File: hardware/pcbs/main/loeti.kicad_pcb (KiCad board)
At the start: 4 copper layers, 80 x 50.5 mm, 99 parts, among them J1 REDFIT_SWD_6, J2 DATA, J3 POWER, J4 Conn_01x04_Pin, Q1 Si4162DY, Q2 BC817, Q4 BC817, Q5 BC807, Q6 Si4425FDY, SW1 BOOT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

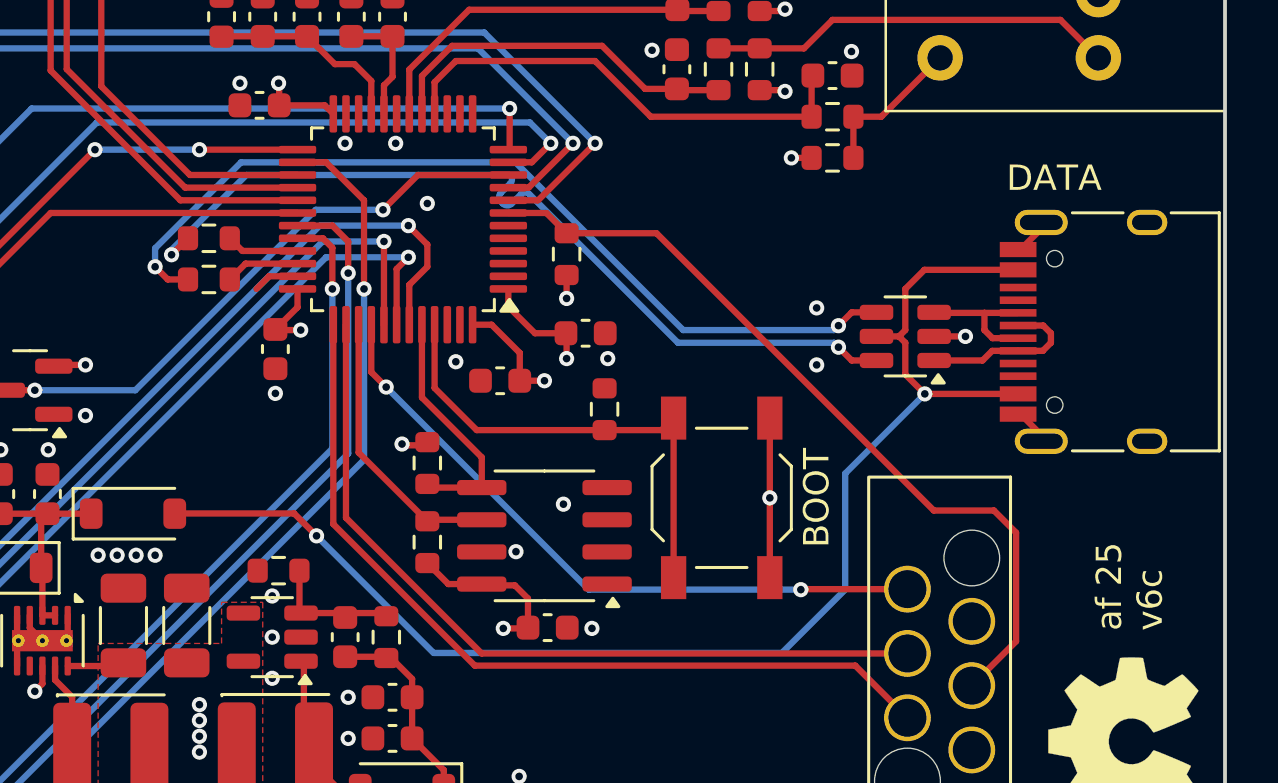
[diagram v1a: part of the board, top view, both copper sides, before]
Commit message: fix: v6d hardware, CC resistors on data port
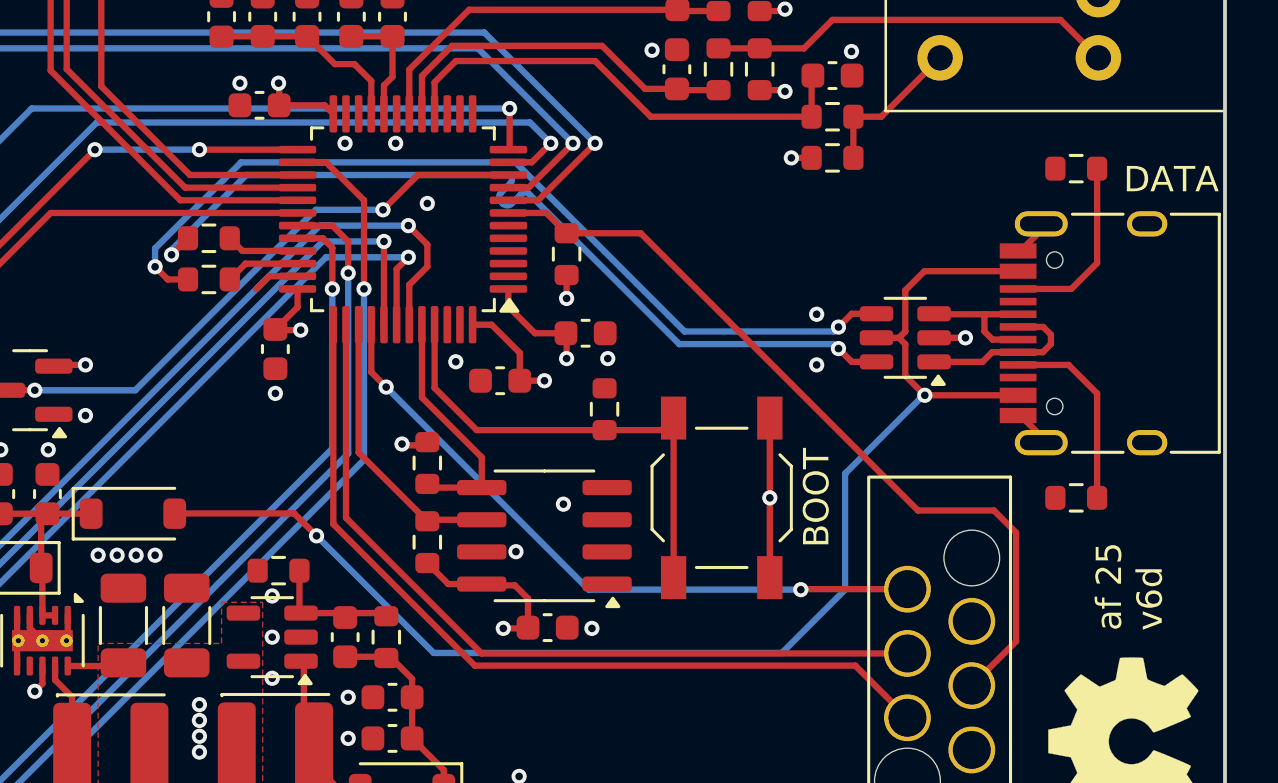
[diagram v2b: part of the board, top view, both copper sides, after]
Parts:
- added R33: 5.1k, Resistor_SMD:R_0603_1608Metric, F.Cu at (181.0, 102.2)
- added R34: 5.1k, Resistor_SMD:R_0603_1608Metric, F.Cu at (181.0, 89.2)
- moved J2 0.06 mm to (182.8, 95.8)
- moved U1 0.06 mm to (174.2, 95.9)
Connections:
- J2 pad A5: unconnected-(J2-CC1-PadA5) -> Net-(J2-CC1)
- J2 pad B5: unconnected-(J2-CC2-PadB5) -> Net-(J2-CC2)
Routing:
- net Net-(J2-CC1): track 0.00 -> 7.71 mm
- net Net-(J2-CC2): track 0.00 -> 7.27 mm
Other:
- board text added: "af 25 v6d"
- board text removed: "af 25 v6c"

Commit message: feat: sleep support on PCB
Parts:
- added D9: BAT54S, Package_TO_SOT_SMD:SOT-23, F.Cu at (167.0, 89.5)
- added R35: 10k, Resistor_SMD:R_0603_1608Metric, F.Cu at (164.2, 89.0)
- added R36: 10k, Resistor_SMD:R_0603_1608Metric, F.Cu at (167.0, 92.5)
- added TP1: SLP, TestPoint:TestPoint_Plated_Hole_D2.0mm, F.Cu at (175.2, 89.8)
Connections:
- net /ADC2_IN1 renamed /ADC1_IN1
- net /ADC2_IN2 renamed /ADC1_IN2
- R34 pad 1: GND -> Net-(J2-CC2)
- R34 pad 2: Net-(J2-CC2) -> GND
- U4 pad 13: unconnected-(U4-PA5-Pad13) -> /SLP
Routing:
- net Net-(R35-Pad1): track 0.00 -> 14.7 mm
- net /SLP: track 0.00 -> 12.3 mm
- net +3V3: track 58.0 -> 61.2 mm, vias 25 -> 26
- net GND: vias 54 -> 55

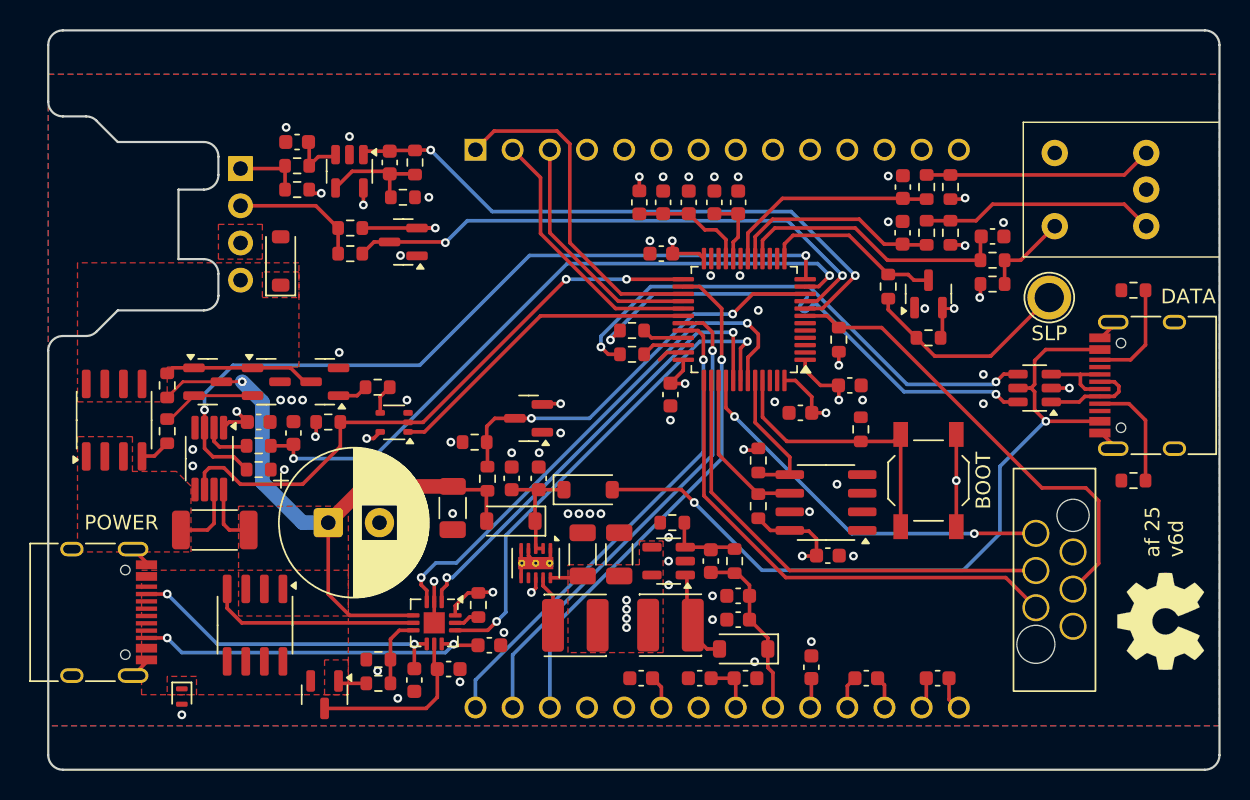
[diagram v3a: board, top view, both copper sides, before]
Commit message: feat: update to 5-pin XLR for sleep
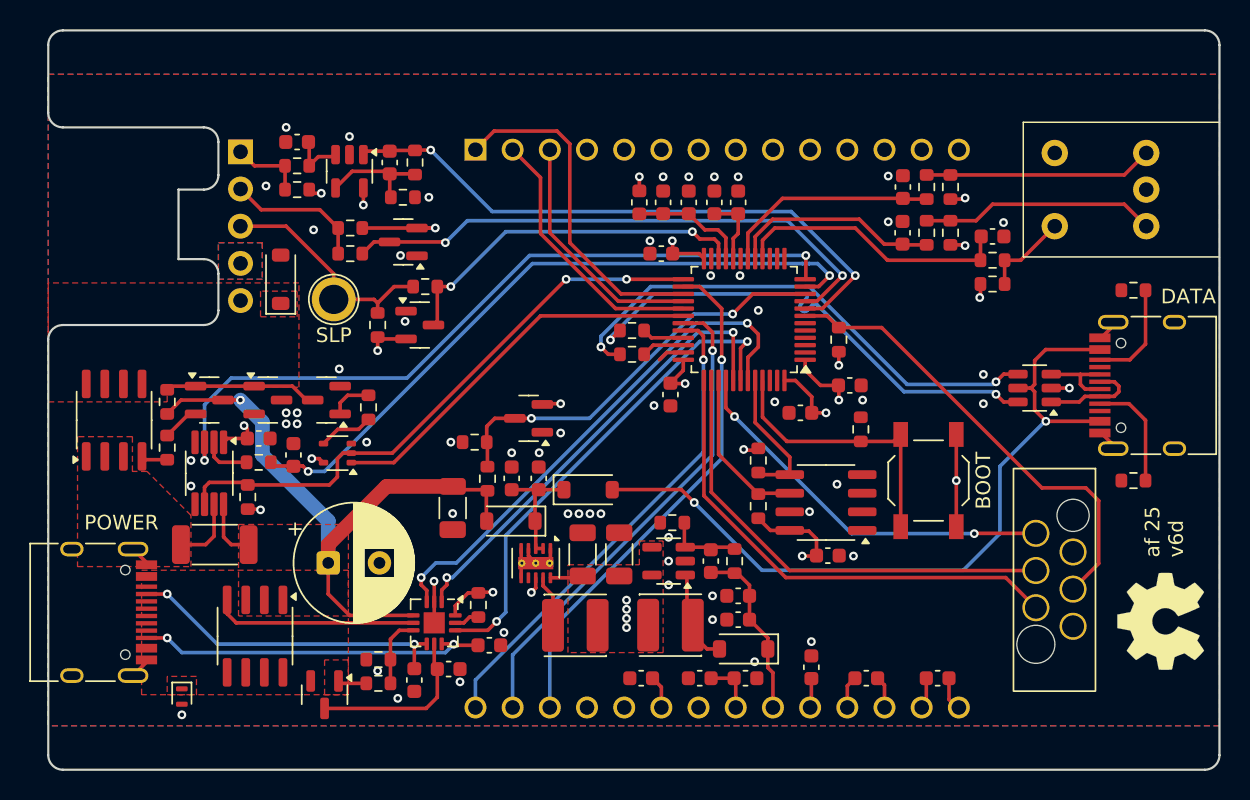
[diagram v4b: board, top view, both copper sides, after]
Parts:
- removed J4: Conn_01x04_Pin, Connector_PinHeader_2.54mm:PinHeader_1x04_P2.54mm_Horizontal
- removed R29: 25k, Resistor_SMD:R_0603_1608Metric
- added J5: Conn_01x05_Pin, Connector_PinHeader_2.54mm:PinHeader_1x05_P2.54mm_Horizontal, B.Cu at (120.0, 79.8)
- C26: footprint Capacitor_THT:CP_Radial_D10.0mm_P3.50mm -> Capacitor_THT:CP_Radial_D8.0mm_P3.50mm
- moved TP1 48.9 mm to (126.4, 89.9)
- moved R36 37.6 mm to (129.4, 91.6), turned to 90 degrees
- moved D9 34.8 mm to (132.2, 91.6), turned to 0 degrees
- moved R35 31.6 mm to (132.6, 89.0), turned to 0 degrees
- moved R30 7.52 mm to (120.5, 103.4), turned to -90 degrees
- moved U6 4.41 mm to (126.6, 100.4)
- moved C26 2.75 mm to (126.0, 107.9)
- moved R22 1.51 mm to (128.8, 97.2), turned to 90 degrees
- moved C33 1.50 mm to (123.6, 100.5)
- moved Q2 1.25 mm to (117.9, 96.8)
- moved Q4 1.25 mm to (125.9, 96.8)
- moved Q5 1.25 mm to (121.9, 96.8)
- moved D5 1.25 mm to (122.8, 88.5)
- moved C34 1.12 mm to (121.2, 99.4)
- moved R18 1.12 mm to (115.0, 96.9)
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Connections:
- net Net-(R35-Pad1) renamed /SLP_EXT
- U4 pad 13: /SLP -> unconnected-(U4-PA5-Pad13)
- U4 pad 22: unconnected-(U4-PB10-Pad22) -> /SLP
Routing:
- net /SLP: track 12.3 -> 24.9 mm, vias 0 -> 2
- net /TIM1_CH1: track 22.1 -> 26.8 mm
- net Net-(Q2-E): track 6.26 -> 2.09 mm
- net Net-(R22-Pad1): track 2.02 -> 3.76 mm
- net /DAC1_OUT1: track 53.7 -> 52.0 mm
- net /SLP_EXT: track 14.7 -> 16.1 mm
- net /CURR_ALERT: track 41.2 -> 40.4 mm
- net +3V3: track 61.2 -> 60.5 mm
- net VDC: track 47.8 -> 47.0 mm
- net /TC+: track 4.35 -> 5.06 mm
- net Net-(Q4-B): track 2.08 -> 2.66 mm
- net Net-(Q1-G): track 14.4 -> 13.9 mm
- net GND: vias 55 -> 57
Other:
- outline, holes or cut-outs redrawn
- board text added: "+14,500 mm from center"
- board text added: "-1,000 mm from center"
- board text added: "-11,875 mm from center"
- board text added: "-14,375 mm from center"

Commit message: feat: v7a initial hardware design
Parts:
- removed C30: ~, Capacitor_SMD:C_0603_1608Metric
- removed U11: TLV333DBV, Package_TO_SOT_SMD:SOT-23-5
- added C2: 100n, Capacitor_SMD:C_0603_1608Metric, F.Cu at (133.4, 85.2)
- added D10: BAT54S, Package_TO_SOT_SMD:SOT-23, F.Cu at (138.1, 85.3)
- added R29: 220k, Resistor_SMD:R_0603_1608Metric, F.Cu at (126.0, 91.1)
- added R37: 220k, Resistor_SMD:R_0603_1608Metric, F.Cu at (126.9, 85.2)
- added R38: 1k, Resistor_SMD:R_0603_1608Metric, F.Cu at (130.1, 85.2)
- added U7: TLV2333, Package_SO:SOIC-8_3.9x4.9mm_P1.27mm, F.Cu at (131.8, 88.9)
- C29: value 330p -> 22p
- Q6: value Si4425FDY -> Si4825
- R23: value 1M -> 22k
- R24: value 10k -> 22k
- R26: value 1k -> 10k
- moved D9 13.4 mm to (130.2, 78.4)
- moved R35 13.4 mm to (130.6, 75.8)
- moved R36 13.4 mm to (127.4, 78.4)
- moved C29 11.5 mm to (138.1, 88.9)
- moved TP1 11.4 mm to (124.0, 78.8), turned to 180 degrees
- moved R26 10.5 mm to (139.8, 88.9), turned to 90 degrees
- moved R25 9.52 mm to (136.5, 88.9), turned to 90 degrees
- moved R23 7.32 mm to (126.0, 89.4)
- moved D2 5.06 mm to (127.2, 82.7)
- moved R10 5.06 mm to (123.6, 83.5)
- moved R9 5.06 mm to (123.6, 81.8)
- moved R24 4.51 mm to (123.6, 85.2)
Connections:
- C29 pad 1: /ADC1_IN1 -> /ADC1_IN2
- C29 pad 2: Net-(U11--) -> Net-(U7B--)
- D2 pad 3: /ADC1_IN2 -> /ADC1_IN1
- D5 pad 1: /HEATER -> /RED
- J5 pad 1: /TC+ -> /SLP_EXT
- J5 pad 3: /SLP_EXT -> /GREEN
- J5 pad 5: /HEATER -> /RED
- Q6 pad 5: /HEATER -> /RED
- Q6 pad 6: /HEATER -> /RED
- Q6 pad 7: /HEATER -> /RED
- Q6 pad 8: /HEATER -> /RED
- R10 pad 2: /ADC1_IN2 -> /ADC1_IN1
- R23 pad 1: +3V3 -> Net-(U7A-+)
- R23 pad 2: /TC+ -> /RED
- R24 pad 1: /TC+ -> /GREEN
- R25 pad 1: /ADC1_IN1 -> Net-(U7B--)
- R25 pad 2: Net-(U11--) -> /ADC1_IN2
- R26 pad 1: Net-(U11--) -> Net-(U7B--)
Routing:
- net Net-(U7B-+): track 0.00 -> 9.20 mm
- net Net-(U11--): track 7.42 -> 0.00 mm
- net Net-(U7B--): track 0.00 -> 5.71 mm
- net /TC+: track 5.06 -> 0.00 mm
- net /DET: track 9.32 -> 4.58 mm
- net /SLP: track 24.9 -> 29.6 mm
- net Net-(U7A-+): track 0.00 -> 4.26 mm
- net /SLP_EXT: track 16.1 -> 11.9 mm
- net Net-(R37-Pad2): track 0.00 -> 3.33 mm
- net Net-(U7A--): track 3.52 -> 6.83 mm
- net /ADC1_IN2: track 38.6 -> 35.4 mm
- net /ADC1_IN1: track 41.5 -> 44.5 mm
- net /GREEN: track 0.00 -> 2.96 mm
- net /RED: track 0.00 -> 2.75 mm
- net +3V3: track 60.5 -> 61.6 mm
- added copper zone on F.Cu, net /RED
- removed copper zone on F.Cu, net /HEATER
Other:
- board text added: "af 25 v7a"
- board text removed: "af 25 v6d"

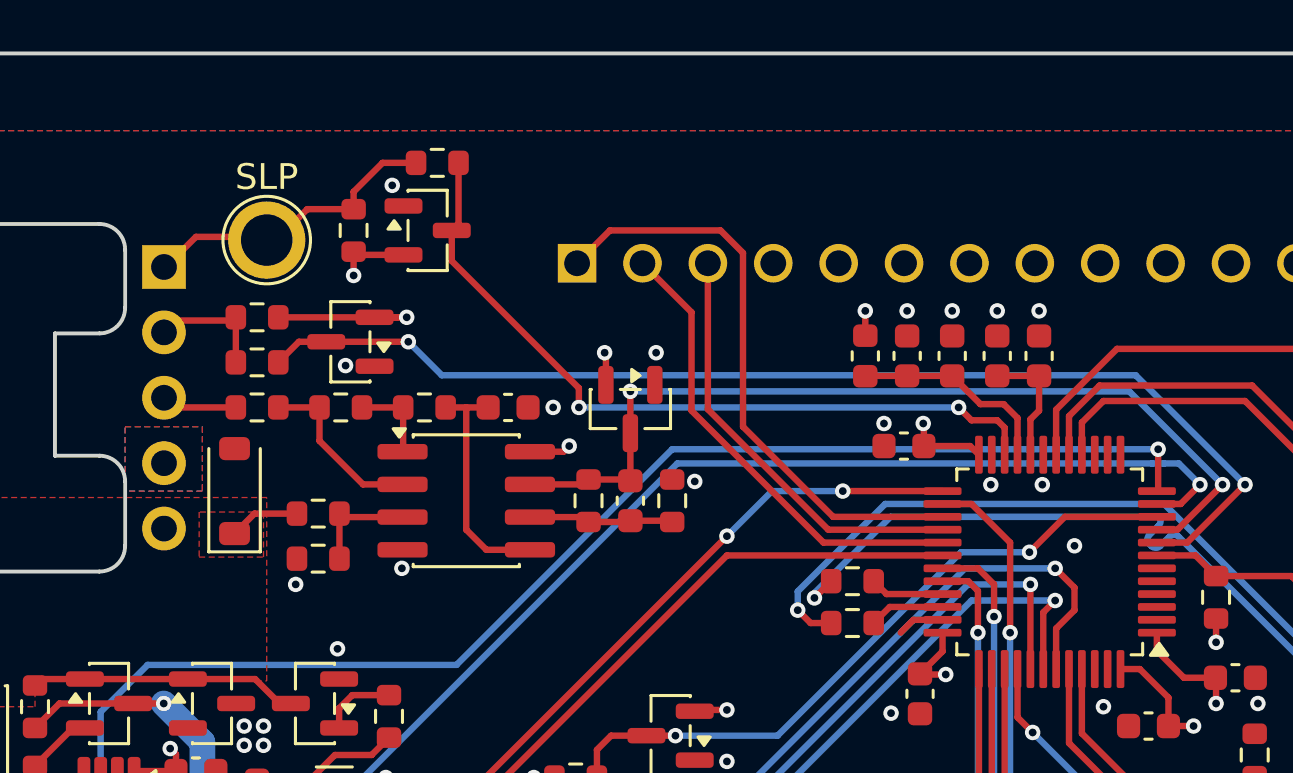
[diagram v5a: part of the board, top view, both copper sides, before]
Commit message: feat: support multiple board variants
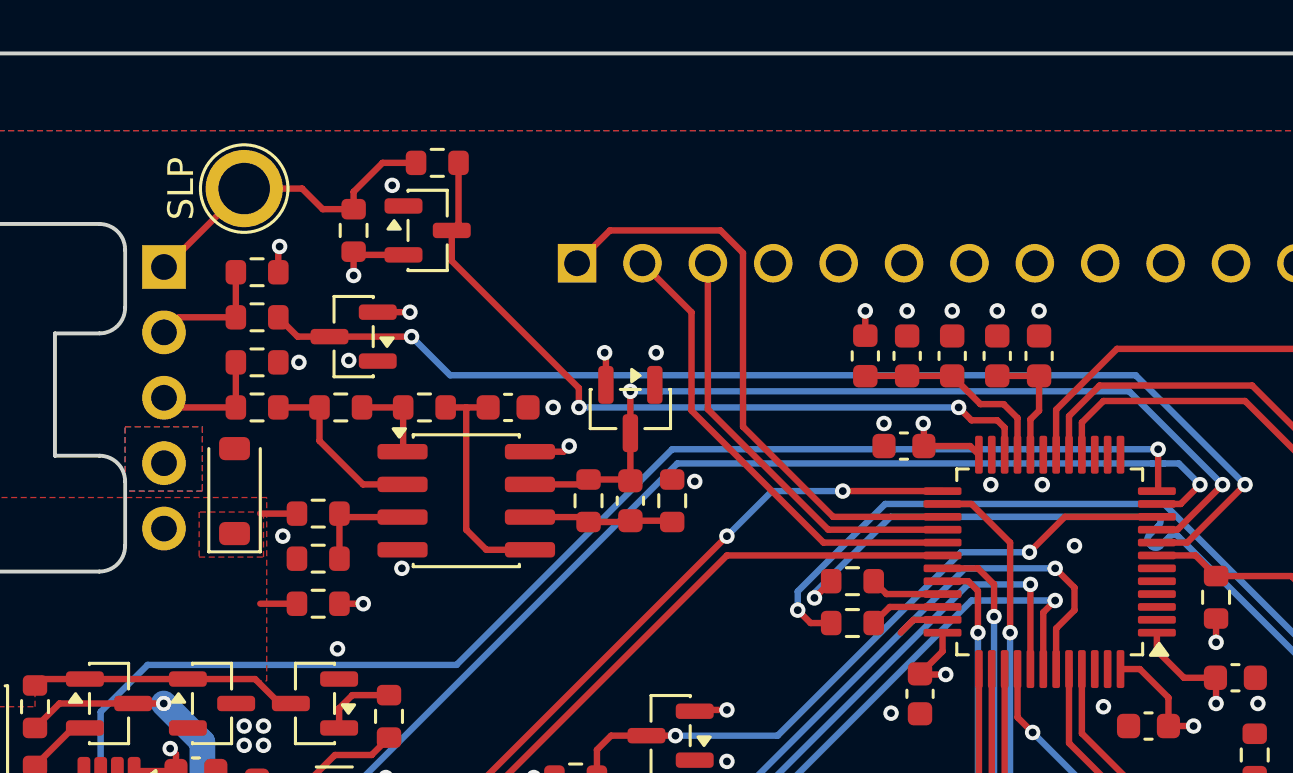
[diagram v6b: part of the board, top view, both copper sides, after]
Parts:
- added R39: 2M, Resistor_SMD:R_0603_1608Metric, F.Cu at (123.6, 83.5)
- added R40: 2M, Resistor_SMD:R_0603_1608Metric, F.Cu at (126.0, 92.9)
- moved TP1 2.18 mm to (123.1, 76.8), turned to -90 degrees
- moved R10 1.75 mm to (123.6, 81.8)
- moved R9 1.75 mm to (123.6, 80.0)
- moved D2 0.24 mm to (127.4, 82.5)
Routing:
- net +3V3: track 61.6 -> 58.8 mm, vias 26 -> 28
- net /GREEN: track 2.96 -> 4.71 mm
- net /SLP_EXT: track 11.9 -> 12.5 mm
- net GND: track 14.6 -> 14.5 mm, vias 57 -> 58

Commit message: feat: hw v7a
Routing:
- net Net-(Q2-E): track 2.09 -> 6.09 mm
- net Net-(U7B--): track 5.71 -> 5.13 mm
- net /GREEN: track 4.71 -> 4.17 mm
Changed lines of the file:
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@@
 			)
 		)
-		(property "Datasheet" "https://www.st.com/resource/en/datasheet/stm32g431cb.pdf"
+		(property "Datasheet" "https://www.st.com/resource/en/datasheet/stm32g491cc.pdf"
 			(at 0 0 0)
 			(layer "F.Fab")
@@
 			)
 		)
-		(property "Description" "STMicroelectronics Arm Cortex-M4 MCU, 128KB flash, 32KB RAM, 170 MHz, 1.71-3.6V, 38 GPIO, LQFP48"
+		(property "Description" "STMicroelectronics Arm Cortex-M4 MCU, 256KB flash, 112KB RAM, 170 MHz, 1.71-3.6V, 38 GPIO, LQFP48"
 			(at 0 0 0)
 			(layer "F.Fab")
@@
 	)
 	(segment
-		(start 129.25 90.805)
-		(end 129.275 90.78)
-		(width 0.25)
-		(layer "F.Cu")
-		(net 2)
-	)
-	(segment
 		(start 175.3875 95.93)
 		(end 176.625 95.93)
@@
 	)
 	(segment
-		(start 136.425 89.625)
-		(end 136.5 89.7)
-		(width 0.25)
-		(layer "F.Cu")
-		(net 7)
-	)
-	(segment
-		(start 139.75 89.625)
-		(end 139.75 89.7)
-		(width 0.25)
-		(layer "F.Cu")
-		(net 7)
-	)
-	(segment
-		(start 139.725 89.65)
-		(end 139.75 89.625)
-		(width 0.25)
-		(layer "F.Cu")
-		(net 7)
-	)
-	(segment
-		(start 136.185 89.51)
-		(end 136.3 89.625)
-		(width 0.25)
-		(layer "F.Cu")
-		(net 7)
-	)
-	(segment
 		(start 134.225 89.51)
 		(end 136.185 89.51)
@@
 	)
 	(segment
-		(start 138.075 89.7)
-		(end 138.125 89.65)
-		(width 0.25)
-		(layer "F.Cu")
-		(net 7)
-	)
-	(segment
 		(start 136.5 89.7)
 		(end 138.075 89.7)
@@
 	)
 	(segment
-		(start 136.3 89.625)
-		(end 136.425 89.625)
-		(width 0.25)
-		(layer "F.Cu")
-		(net 7)
-	)
-	(segment
 		(start 140.175 106.890661)
 		(end 140.675 106.890661)
@@
 	)
 	(segment
+		(start 120.9375 97.7)
+		(end 116.9375 97.7)
+		(width 0.25)
+		(layer "F.Cu")
+		(net 21)
+	)
+	(segment
 		(start 116.475 97.7)
 		(end 115 99.175)
@@
 	)
 	(segment
-		(start 138.125 88.025)
-		(end 138.125 88.1)
-		(width 0.25)
-		(layer "F.Cu")
-		(net 72)
-	)
-	(segment
-		(start 136.5 88.175)
-		(end 136.5 88.05)
-		(width 0.25)
-		(layer "F.Cu")
-		(net 72)
-	)
-	(segment
 		(start 138.125 84.625)
 		(end 138.125 88.1)
@@
 	)
 	(segment
-		(start 138.1 88.05)
-		(end 138.125 88.025)
-		(width 0.25)
-		(layer "F.Cu")
-		(net 72)
-	)
-	(segment
 		(start 159.375 90)
 		(end 158.575 90)
@@
 		(net 72)
 	)
-	(segment
-		(start 136.435 88.24)
-		(end 136.5 88.175)
-		(width 0.25)
-		(layer "F.Cu")
-		(net 72)
-	)
 	(via
 		(at 138.125 84.625)
@@
 	)
 	(segment
-		(start 120.375 85.25)
-		(end 120 84.875)
-		(width 0.25)
-		(layer "F.Cu")
-		(net 76)
-	)
-	(segment
 		(start 122.8 85.25)
 		(end 120.375 85.25)
@@
 	)
 	(segment
-		(start 120.01 79.795)
-		(end 120.08 79.795)
-		(width 0.25)
-		(layer "F.Cu")
-		(net 95)
-	)
-	(segment
 		(start 126.175 77.55)
 		(end 125.375 76.75)
@@
 	)
 	(segment
-		(start 126.96 89.51)
-		(end 126.825 89.375)
-		(width 0.25)
-		(layer "F.Cu")
-		(net 96)
-	)
-	(segment
 		(start 126.825 91.125)
 		(end 126.825 89.375)
@@
 		(net 98)
 	)
-	(segment
-		(start 129.3 86.945)
-		(end 129.275 86.97)
-		(width 0.25)
-		(layer "F.Cu")
-		(net 98)
-	)
 	(zone
 		(net 3)
@@
 			(pts
 				(xy 116.625 104.625) (xy 113.625 101.625) (xy 112.625 101.625) (xy 112.625 99.25) (xy 108.875 99.25)
-				(xy 108.875 108.125) (xy 116.625 108.125)
+				(xy 108.875 108.125) (xy 114.75 108.125) (xy 116.625 108.125)
 			)
 		)
